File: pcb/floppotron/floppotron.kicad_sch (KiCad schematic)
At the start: 62 parts, among them J1 DIN-5_180degree, J10 Power, J2 Conn_01x02, J3 Conn_01x02, J4 Conn_01x02, J5 Conn_01x02, J6 Conn_01x02, J7 Conn_01x02, J9 USB_B, Q1 BC817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

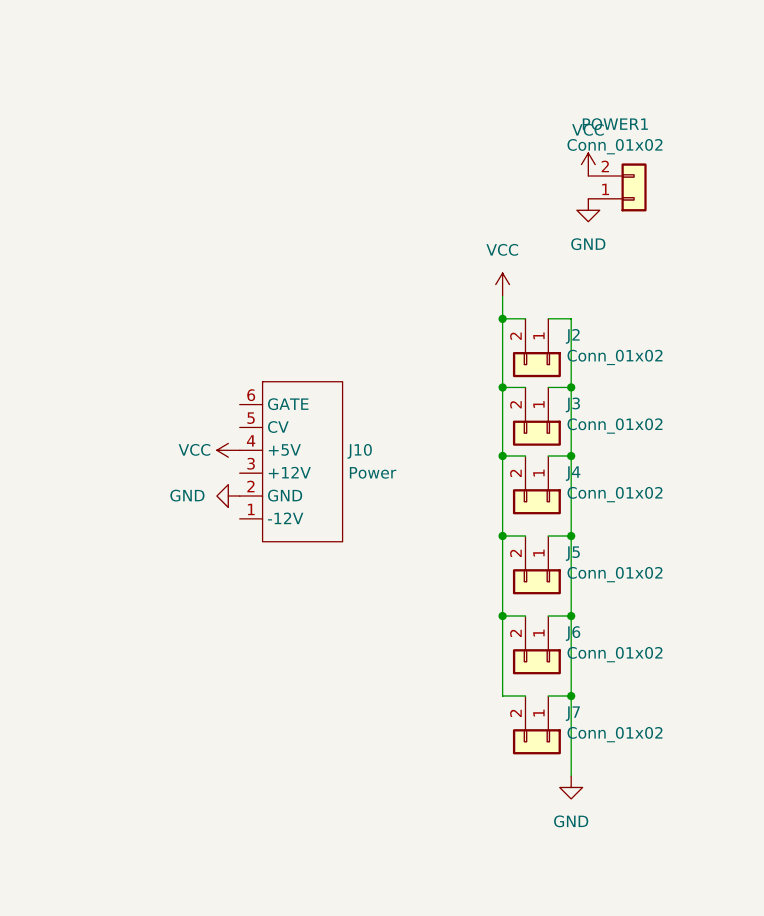
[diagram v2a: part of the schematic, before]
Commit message: clean up traces
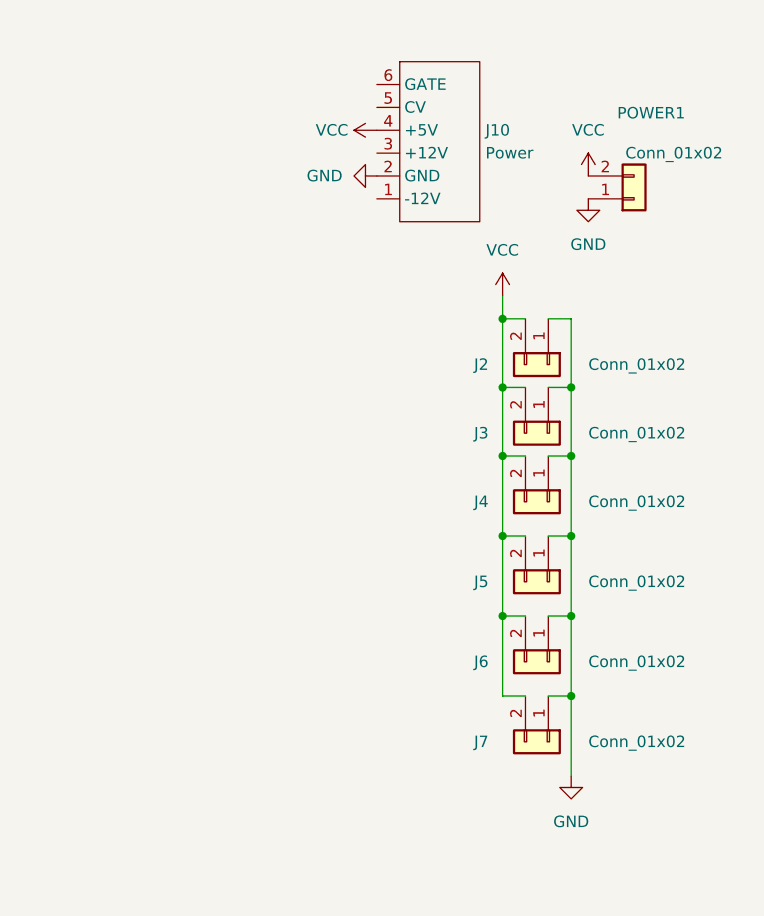
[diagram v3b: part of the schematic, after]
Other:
- moved on the sheet: J10
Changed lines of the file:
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@@
   (symbol (lib_id "Connector_Generic:Conn_01x02") (at 271.78 36.83 0) (mirror x) (unit 1)
     (in_bom yes) (on_board yes) (dnp no)
-    (property "Reference" "POWER1" (at 269.6972 28.575 0)
+    (property "Reference" "POWER1" (at 273.685 27.305 0)
       (effects (font (size 1.27 1.27)))
     )
-    (property "Value" "Conn_01x02" (at 269.6972 30.8864 0)
+    (property "Value" "Conn_01x02" (at 276.225 31.75 0)
       (effects (font (size 1.27 1.27)))
     )
@@
   (symbol (lib_id "Connector_Generic:Conn_01x02") (at 262.255 55.245 270) (unit 1)
     (in_bom yes) (on_board yes) (dnp no)
-    (property "Reference" "J2" (at 264.287 51.9938 90)
-      (effects (font (size 1.27 1.27)) (justify left))
-    )
-    (property "Value" "Conn_01x02" (at 264.287 54.3052 90)
+    (property "Reference" "J2" (at 254 55.245 90)
+      (effects (font (size 1.27 1.27)) (justify left))
+    )
+    (property "Value" "Conn_01x02" (at 266.7 55.245 90)
       (effects (font (size 1.27 1.27)) (justify left))
     )
@@
   (symbol (lib_id "Connector_Generic:Conn_01x02") (at 262.255 62.865 270) (unit 1)
     (in_bom yes) (on_board yes) (dnp no)
-    (property "Reference" "J3" (at 264.287 59.6138 90)
-      (effects (font (size 1.27 1.27)) (justify left))
-    )
-    (property "Value" "Conn_01x02" (at 264.287 61.9252 90)
+    (property "Reference" "J3" (at 254 62.865 90)
+      (effects (font (size 1.27 1.27)) (justify left))
+    )
+    (property "Value" "Conn_01x02" (at 266.7 62.865 90)
       (effects (font (size 1.27 1.27)) (justify left))
     )
@@
   (symbol (lib_id "Connector_Generic:Conn_01x02") (at 262.255 70.485 270) (unit 1)
     (in_bom yes) (on_board yes) (dnp no)
-    (property "Reference" "J4" (at 264.287 67.2338 90)
-      (effects (font (size 1.27 1.27)) (justify left))
-    )
-    (property "Value" "Conn_01x02" (at 264.287 69.5452 90)
+    (property "Reference" "J4" (at 254 70.485 90)
+      (effects (font (size 1.27 1.27)) (justify left))
+    )
+    (property "Value" "Conn_01x02" (at 266.7 70.485 90)
       (effects (font (size 1.27 1.27)) (justify left))
     )
@@
   (symbol (lib_id "Connector_Generic:Conn_01x02") (at 262.255 79.375 270) (unit 1)
     (in_bom yes) (on_board yes) (dnp no)
-    (property "Reference" "J5" (at 264.287 76.1238 90)
-      (effects (font (size 1.27 1.27)) (justify left))
-    )
-    (property "Value" "Conn_01x02" (at 264.287 78.4352 90)
+    (property "Reference" "J5" (at 254 79.375 90)
+      (effects (font (size 1.27 1.27)) (justify left))
+    )
+    (property "Value" "Conn_01x02" (at 266.7 79.375 90)
       (effects (font (size 1.27 1.27)) (justify left))
     )
@@
   (symbol (lib_id "Connector_Generic:Conn_01x02") (at 262.255 88.265 270) (unit 1)
     (in_bom yes) (on_board yes) (dnp no)
-    (property "Reference" "J6" (at 264.287 85.0138 90)
-      (effects (font (size 1.27 1.27)) (justify left))
-    )
-    (property "Value" "Conn_01x02" (at 264.287 87.3252 90)
+    (property "Reference" "J6" (at 254 88.265 90)
+      (effects (font (size 1.27 1.27)) (justify left))
+    )
+    (property "Value" "Conn_01x02" (at 266.7 88.265 90)
       (effects (font (size 1.27 1.27)) (justify left))
     )
@@
   (symbol (lib_id "Connector_Generic:Conn_01x02") (at 262.255 97.155 270) (unit 1)
     (in_bom yes) (on_board yes) (dnp no)
-    (property "Reference" "J7" (at 264.287 93.9038 90)
-      (effects (font (size 1.27 1.27)) (justify left))
-    )
-    (property "Value" "Conn_01x02" (at 264.287 96.2152 90)
+    (property "Reference" "J7" (at 254 97.155 90)
+      (effects (font (size 1.27 1.27)) (justify left))
+    )
+    (property "Value" "Conn_01x02" (at 266.7 97.155 90)
       (effects (font (size 1.27 1.27)) (justify left))
     )
@@
     )
   )
-  (symbol (lib_id "kosmo:Power-16") (at 234.315 66.04 0) (unit 1)
+  (symbol (lib_id "kosmo:Power-16") (at 249.555 30.48 0) (unit 1)
     (in_bom yes) (on_board yes) (dnp no) (fields_autoplaced)
-    (property "Reference" "J10" (at 240.03 64.77 0)
-      (effects (font (size 1.27 1.27)) (justify left))
-    )
-    (property "Value" "Power" (at 240.03 67.31 0)
-      (effects (font (size 1.27 1.27)) (justify left))
-    )
-    (property "Footprint" "kosmo:Power 16 Pin" (at 240.665 63.5 90)
-      (effects (font (size 1.27 1.27)) hide)
-    )
-    (property "Datasheet" "" (at 236.855 59.69 0)
+    (property "Reference" "J10" (at 255.27 29.21 0)
+      (effects (font (size 1.27 1.27)) (justify left))
+    )
+    (property "Value" "Power" (at 255.27 31.75 0)
+      (effects (font (size 1.27 1.27)) (justify left))
+    )
+    (property "Footprint" "kosmo:Power 16 Pin" (at 255.905 27.94 90)
+      (effects (font (size 1.27 1.27)) hide)
+    )
+    (property "Datasheet" "" (at 252.095 24.13 0)
       (effects (font (size 1.27 1.27)) hide)
     )
@@
     )
   )
-  (symbol (lib_id "power:GND") (at 227.965 69.85 270) (unit 1)
+  (symbol (lib_id "power:GND") (at 243.205 34.29 270) (unit 1)
     (in_bom yes) (on_board yes) (dnp no) (fields_autoplaced)
-    (property "Reference" "#PWR022" (at 221.615 69.85 0)
-      (effects (font (size 1.27 1.27)) hide)
-    )
-    (property "Value" "GND" (at 224.155 69.85 90)
+    (property "Reference" "#PWR022" (at 236.855 34.29 0)
+      (effects (font (size 1.27 1.27)) hide)
+    )
+    (property "Value" "GND" (at 239.395 34.29 90)
       (effects (font (size 1.27 1.27)) (justify right))
     )
-    (property "Footprint" "" (at 227.965 69.85 0)
-      (effects (font (size 1.27 1.27)) hide)
-    )
-    (property "Datasheet" "" (at 227.965 69.85 0)
+    (property "Footprint" "" (at 243.205 34.29 0)
+      (effects (font (size 1.27 1.27)) hide)
+    )
+    (property "Datasheet" "" (at 243.205 34.29 0)
       (effects (font (size 1.27 1.27)) hide)
     )
@@
     )
   )
-  (symbol (lib_id "power:VCC") (at 227.965 64.77 90) (unit 1)
+  (symbol (lib_id "power:VCC") (at 243.205 29.21 90) (unit 1)
     (in_bom yes) (on_board yes) (dnp no) (fields_autoplaced)
-    (property "Reference" "#PWR023" (at 231.775 64.77 0)
-      (effects (font (size 1.27 1.27)) hide)
-    )
-    (property "Value" "VCC" (at 224.79 64.77 90)
-      (effects (font (size 1.27 1.27)) (justify left))
-    )
-    (property "Footprint" "" (at 227.965 64.77 0)
-      (effects (font (size 1.27 1.27)) hide)
-    )
-    (property "Datasheet" "" (at 227.965 64.77 0)
-      (effects (font (size 1.27 1.27)) hide)
-    )
+    (property "Reference" "#PWR023" (at 247.015 29.21 0)
+      (effects (font (size 1.27 1.27)) hide)
+    )
+    (property "Value" "VCC" (at 240.03 29.21 90)
+      (effects (font (size 1.27 1.27)) (justify left))
+    )
+    (property "Footprint" "" (at 243.205 29.21 0)
+      (effects (font (size 1.27 1.27)) hide)
+    )
+    (property "Datasheet" "" (at 243.205 29.21 0)
+      (effects (font (size 1.27 1.27)) hide)
+    )

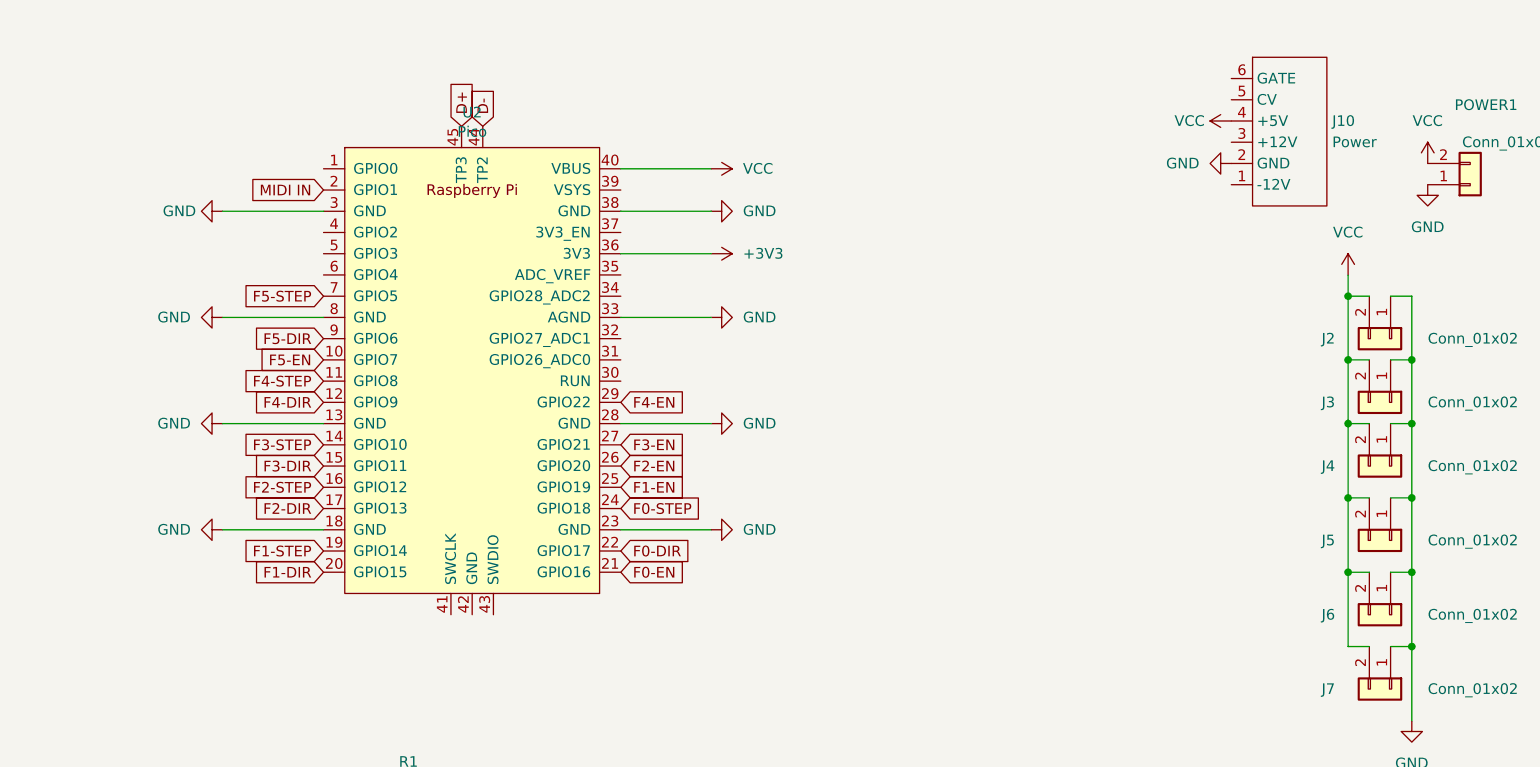
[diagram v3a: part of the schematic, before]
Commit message: pcb: adapt for interface board
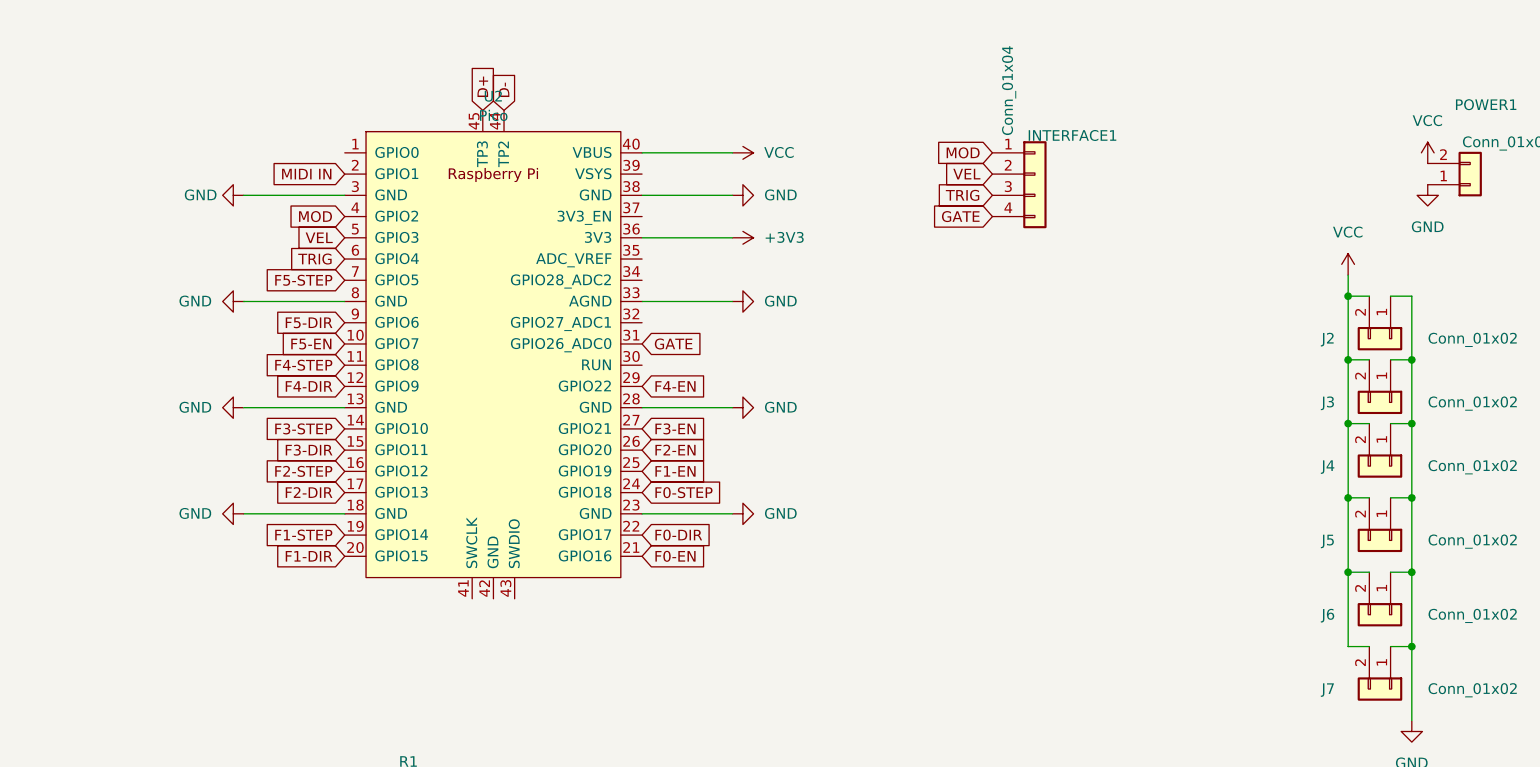
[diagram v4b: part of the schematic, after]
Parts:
- removed J10: Power, kosmo:Power 16 Pin, symbol kosmo:Power-16
- added INTERFACE1: Conn_01x04, Connector_JST:JST_XH_B4B-XH-A_1x04_P2.50mm_Vertical, symbol Connector_Generic:Conn_01x04
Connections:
- net GATE: now reaches U2.31 (GPIO26_ADC0)
- net GATE: now also INTERFACE1.4 (Pin_4)
- net MOD: now reaches U2.4 (GPIO2)
- net MOD: now also INTERFACE1.1 (Pin_1)
- net VEL: now reaches U2.5 (GPIO3)
- net VEL: now also INTERFACE1.2 (Pin_2)
- net TRIG: now reaches U2.6 (GPIO4)
- net TRIG: now also INTERFACE1.3 (Pin_3)
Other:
- moved on the sheet: U2
